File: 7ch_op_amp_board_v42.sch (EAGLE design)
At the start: 12 parts

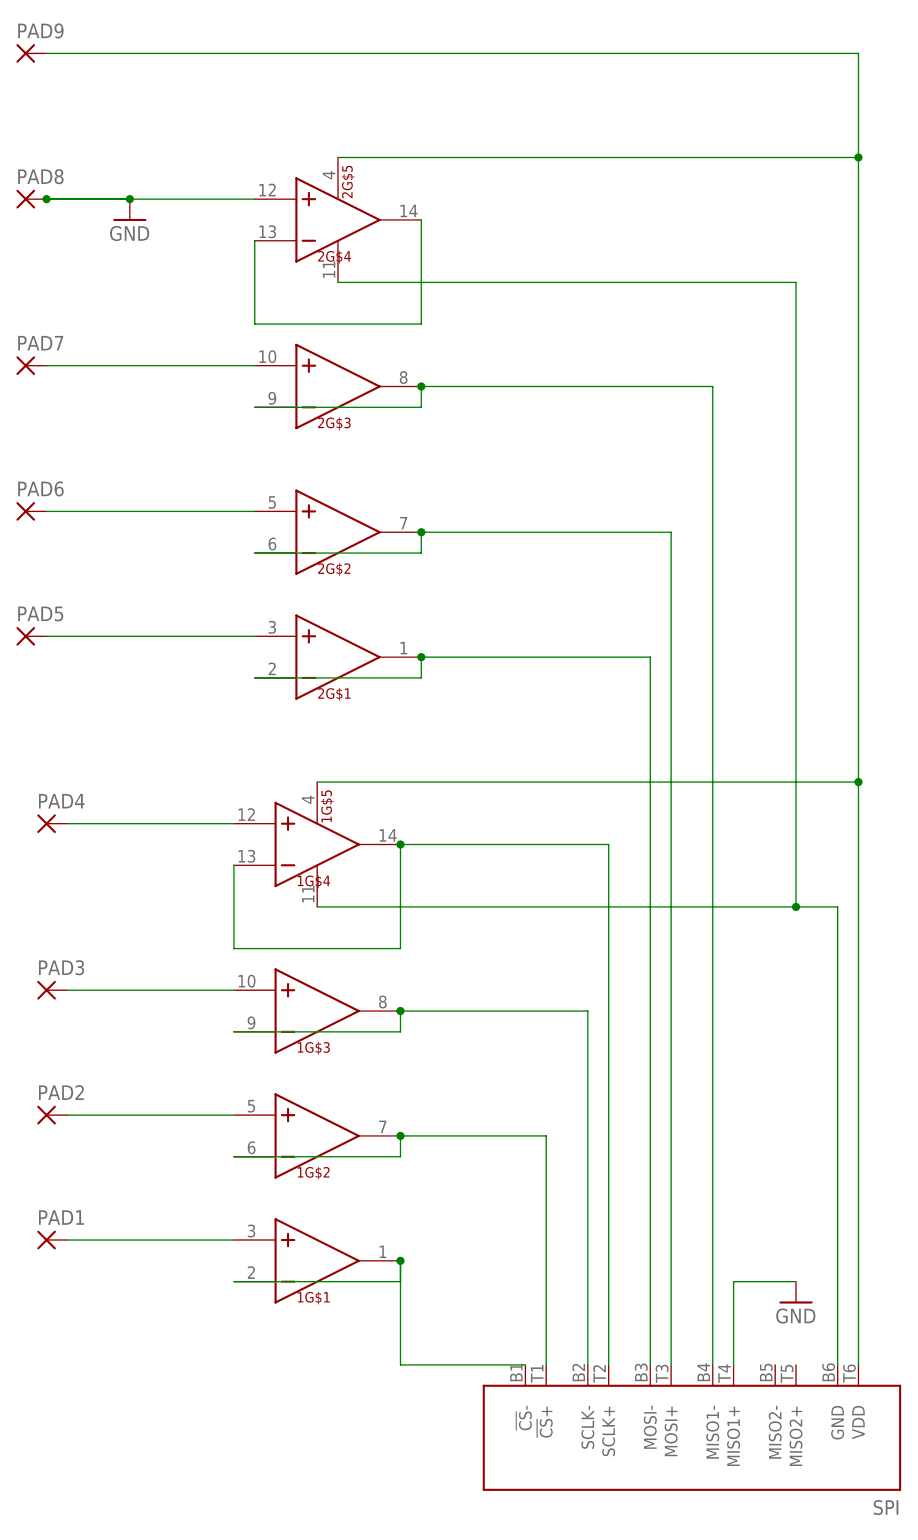
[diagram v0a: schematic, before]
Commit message: Redraw traces to isolate power
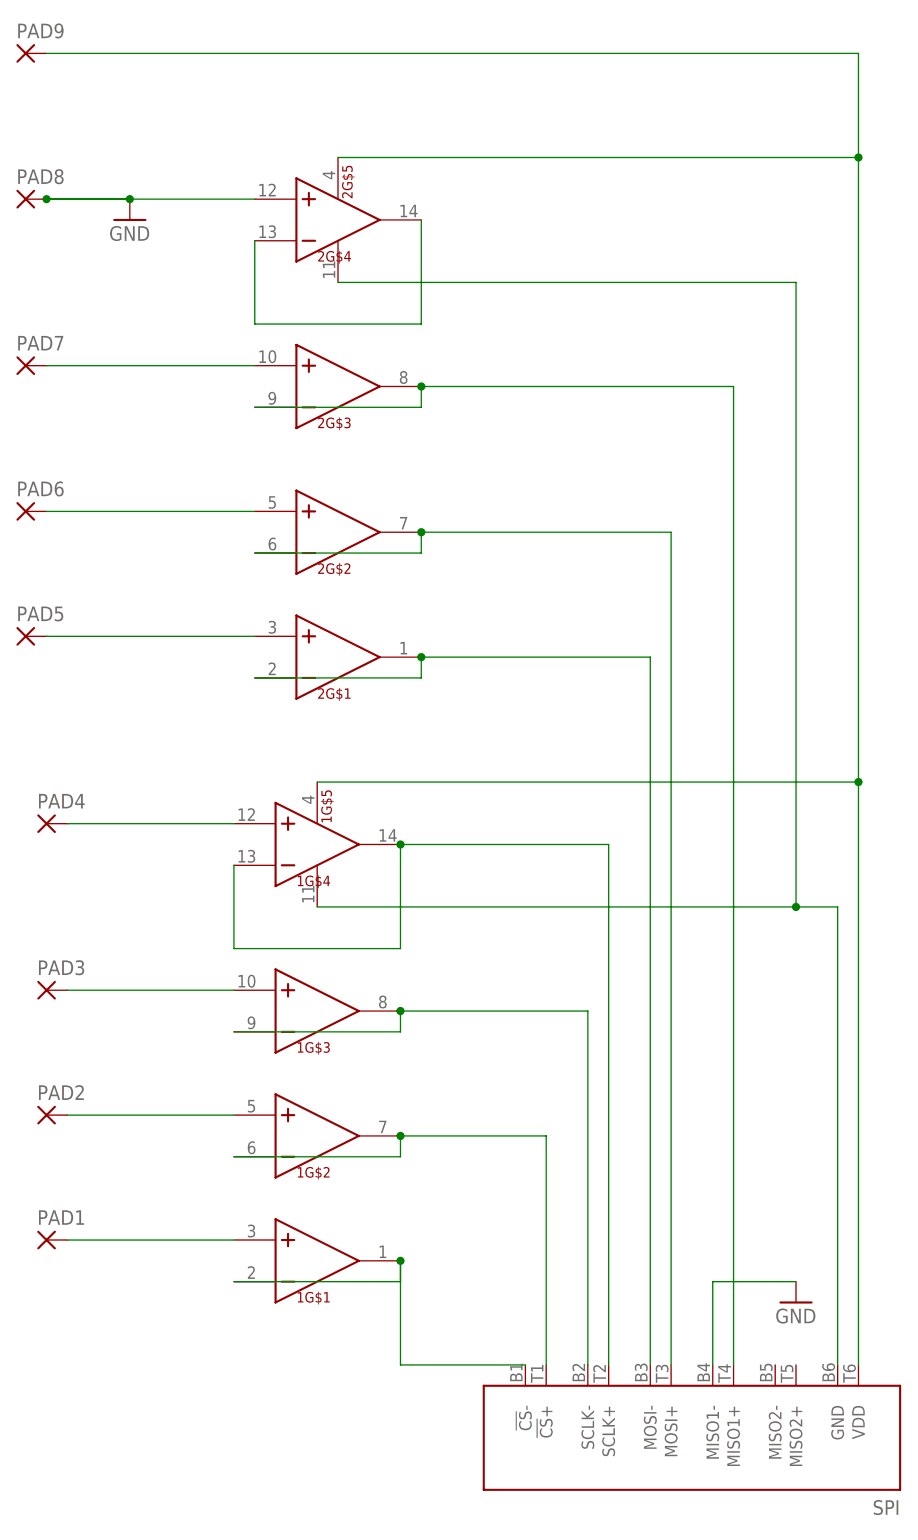
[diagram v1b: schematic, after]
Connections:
- net GND: now also SPI.MISO1-; no longer SPI.MISO1+
- net N$5: now also SPI.MISO1+; no longer SPI.MISO1-
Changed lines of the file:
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@@
 <net name="N$5" class="0">
 <segment>
-<pinref part="SPI" gate="A" pin="MISO1-"/>
-<wire x1="2.54" y1="22.86" x2="2.54" y2="-96.52" width="0.1524" layer="91"/>
 <pinref part="2" gate="G$3" pin="OUT"/>
 <pinref part="2" gate="G$3" pin="IN-"/>
 <wire x1="-53.34" y1="20.32" x2="-33.02" y2="20.32" width="0.1524" layer="91"/>
 <wire x1="-33.02" y1="20.32" x2="-33.02" y2="22.86" width="0.1524" layer="91"/>
-<wire x1="2.54" y1="22.86" x2="-33.02" y2="22.86" width="0.1524" layer="91"/>
+<wire x1="5.08" y1="22.86" x2="-33.02" y2="22.86" width="0.1524" layer="91"/>
 <junction x="-33.02" y="22.86"/>
+<pinref part="SPI" gate="A" pin="MISO1+"/>
+<wire x1="5.08" y1="-96.52" x2="5.08" y2="22.86" width="0.1524" layer="91"/>
 </segment>
 </net>
@@
 <segment>
 <pinref part="GND1" gate="1" pin="GND"/>
-<wire x1="12.7" y1="-86.36" x2="5.08" y2="-86.36" width="0.1524" layer="91"/>
-<pinref part="SPI" gate="A" pin="MISO1+"/>
-<wire x1="5.08" y1="-86.36" x2="5.08" y2="-96.52" width="0.1524" layer="91"/>
+<wire x1="12.7" y1="-86.36" x2="2.54" y2="-86.36" width="0.1524" layer="91"/>
+<pinref part="SPI" gate="A" pin="MISO1-"/>
+<wire x1="2.54" y1="-96.52" x2="2.54" y2="-86.36" width="0.1524" layer="91"/>
 </segment>
 </net>
